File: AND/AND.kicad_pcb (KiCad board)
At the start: 2 copper layers, 20 x 22.5 mm, 7 parts, among them J1 AudioJack2_SwitchT, J2 AudioJack2_SwitchT, J3 AudioJack2_SwitchT, Q1 2N7002, Q2 BSS84, Q3 BSS84

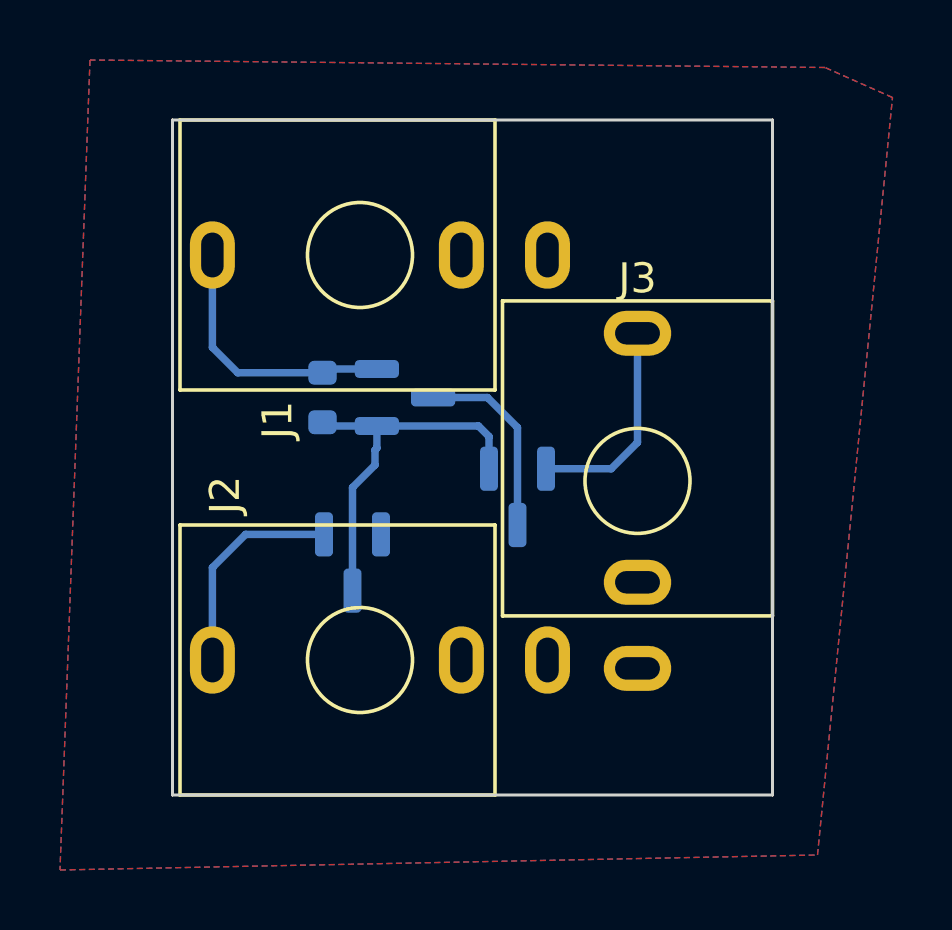
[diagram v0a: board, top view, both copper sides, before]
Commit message: Add AND gate front panel
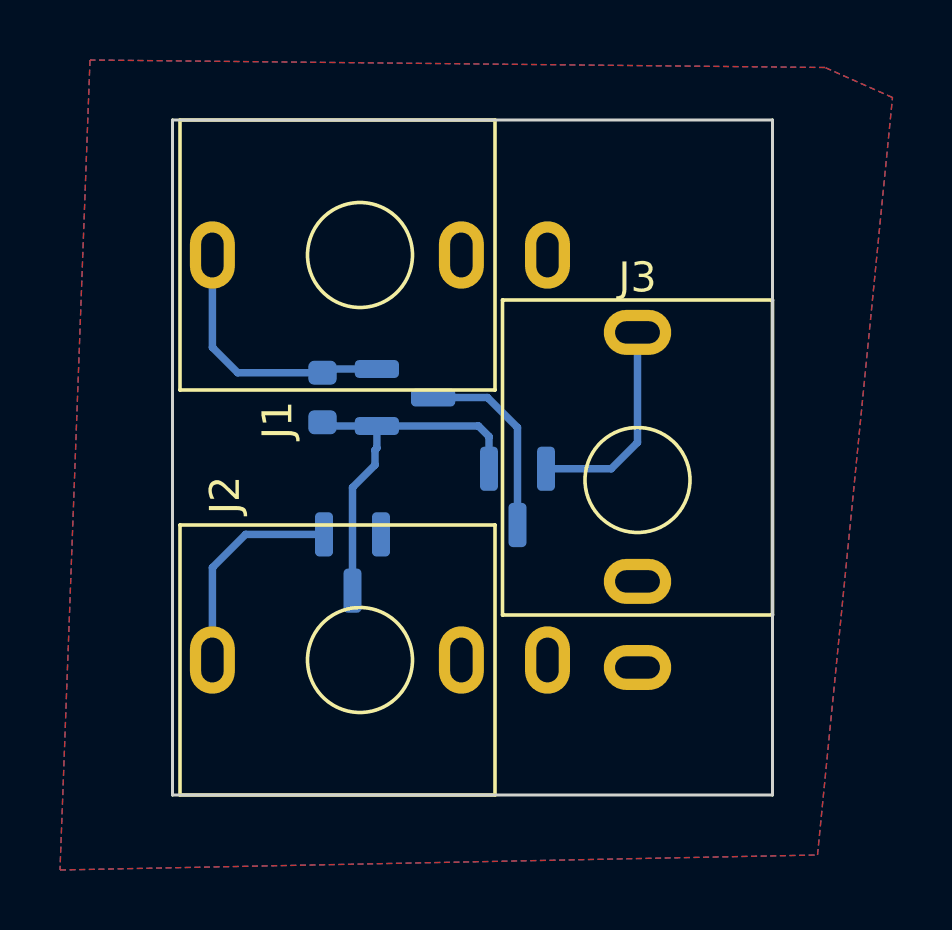
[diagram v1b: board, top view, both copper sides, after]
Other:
- board text added: "Passive AND"
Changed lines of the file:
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@@
 	(footprint "Custom_FP:PJ398SM"
 		(layer "F.Cu")
-		(at 140.5 87.03)
+		(at 140.5 87)
 		(property "Reference" "J3"
 			(at 0 -6.75 0)
@@
 		(tags "SOT TO_SOT_SMD")
 		(property "Reference" "Q3"
-			(at -0.1875 -2.3 360)
+			(at -0.1875 -2.3 0)
 			(layer "B.SilkS")
 			(effects
@@
 		)
 		(property "Value" "BSS84"
-			(at 0 -2.4 360)
+			(at 0 -2.4 0)
 			(layer "B.Fab")
 			(effects
@@
 		)
 		(fp_text user "${REFERENCE}"
-			(at 0 0 360)
+			(at 0 0 0)
 			(layer "B.Fab")
 			(effects
@@
 		(layer "Edge.Cuts")
 	)
+	(gr_text "Passive\nAND"
+		(at 140.75 79.4 0)
+		(layer "B.SilkS")
+		(effects
+			(font
+				(size 1 1)
+				(thickness 0.15)
+			)
+			(justify bottom mirror)
+		)
+	)
 	(segment

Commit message: Improve AND gate off state
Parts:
- added Q4: 2N7002, Package_TO_SOT_SMD:SOT-23, B.Cu at (140.8, 86.2)
- moved Q2 3.29 mm to (136.9, 84.3), turned to 0 degrees
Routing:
- net Net-(Q2-S): track 7.05 -> 10.2 mm
- net Net-(Q1-D): track 12.6 -> 15.7 mm
- net Net-(Q2-D): track 6.48 -> 4.21 mm
